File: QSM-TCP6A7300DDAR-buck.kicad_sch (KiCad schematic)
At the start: 20 parts, among them U1 TCP6A7300DDAR

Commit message: docs: identificar trazos críticos en el esquemático para ruteo
Se agregaron colores y leyendas para diferenciar las pistas de alta corriente (rojo), señales sensibles de retroalimentación (amarillo) y nodos ruidosos con alto dv/dt. Sirve como guía visual obligatoria para el diseño del PCB.
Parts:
- removed U1: TCP6A7300DDAR, Package_SO_ARR:SOIC-8-1EP_3.9x4.9mm_P1.27mm_EP2.29x3mm_ThermalVias, symbol Power_IC_SMD_ARR:TCP6A7300DDAR
- added U1: TCP6A7300DDAR, Package_SO_ARR:SOIC-8-1EP_3.9x4.9mm_P1.27mm_EP2.29x3mm_ThermalVias, symbol SMPS_SMD_ARR:TCP6A7300DDAR
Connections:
- net GND: now also U1.7 (GND), U1.9 (GND)
- net at C5.2, L1.1: now also U1.8 (SW)
- net at C1.1, C2.1, C7.1: now also U1.2 (VIN), U1.3 (EN)
- net at C5.1: now also U1.1 (BOOT)
- net at C6.2, R1.2, R2.1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: now also U1.5 (FB)
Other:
- note added: "HIGH CURRENT TRACES"
- note added: "MOST NOISE SENSITIVE, SMALL SIGNAL TRACES"
- note added: "NOISY, HIGH dv/dt NODES/TRACES"

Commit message: docs: agregar lista de materiales (BOM) y límites de hardware
Se integró la tabla de componentes críticos con enlaces a proveedores locales para ensamble rápido. También se documentaron las consideraciones de derating físico: límite de corriente de 1.4A por saturación del inductor y pérdida de capacitancia por DC bias en los cerámicos 0805.
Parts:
- L1: footprint (none) -> IND_SMD_ARR:IND_SWPA6020S_SNL
- R1: Supplier 1 (none) -> https://uelectronics.com/producto/resistor-56k-ohm-1-8w-smd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
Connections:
- net at C3.1, C4.1, C6.1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: now also R4.1
- no-connect marks 2 -> 1
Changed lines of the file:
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@@
 	)
 	(junction
-		(at 110.49 86.36)
-		(diameter 0)
-		(color 108 0 2 1)
-	)
-	(junction
 		(at 111.76 73.66)
 		(diameter 0)
@@
 	)
 	(junction
+		(at 162.56 81.28)
+		(diameter 0)
+		(color 0 0 0 0)
+	)
+	(junction
 		(at 208.28 76.2)
 		(diameter 0)
@@
 	)
 	(junction
+		(at 162.56 76.2)
+		(diameter 0)
+		(color 108 0 2 1)
+	)
+	(junction
 		(at 162.56 96.52)
 		(diameter 0)
@@
 	)
 	(junction
+		(at 110.49 86.36)
+		(diameter 0)
+		(color 108 0 2 1)
+	)
+	(junction
 		(at 76.2 73.66)
 		(diameter 0)
@@
 	)
 	(junction
-		(at 157.48 76.2)
-		(diameter 0)
-		(color 108 0 2 1)
-	)
-	(junction
 		(at 101.6 73.66)
 		(diameter 0)
@@
 	)
 	(no_connect
-		(at 162.56 81.28)
-	)
-	(no_connect
 		(at 132.08 83.82)
 	)
 	(wire
 		(pts
+			(xy 157.48 81.28) (xy 162.56 81.28)
+		)
+		(stroke
+			(width 0)
+			(type default)
+		)
+	)
+	(wire
+		(pts
 			(xy 132.08 73.66) (xy 133.35 73.66)
 		)
@@
 	(wire
 		(pts
-			(xy 154.94 76.2) (xy 157.48 76.2)
+			(xy 154.94 76.2) (xy 162.56 76.2)
 		)
 		(stroke
@@
 	(wire
 		(pts
-			(xy 110.49 86.36) (xy 110.49 91.44)
+			(xy 110.49 86.36) (xy 110.49 87.63)
 		)
 		(stroke
@@
 	(wire
 		(pts
-			(xy 170.18 96.52) (xy 177.8 96.52)
+			(xy 143.51 71.12) (xy 143.51 76.2)
 		)
 		(stroke
 			(width 0.381)
 			(type default)
-			(color 255 244 0 1)
+			(color 108 0 2 1)
 		)
 	)
 	(wire
 		(pts
-			(xy 143.51 71.12) (xy 143.51 76.2)
+			(xy 208.28 86.36) (xy 208.28 90.17)
 		)
 		(stroke
@@
 	(wire
 		(pts
-			(xy 208.28 86.36) (xy 208.28 90.17)
+			(xy 140.97 71.12) (xy 143.51 71.12)
 		)
 		(stroke
@@
 	(wire
 		(pts
-			(xy 140.97 71.12) (xy 143.51 71.12)
+			(xy 170.18 93.98) (xy 170.18 96.52)
 		)
 		(stroke
 			(width 0.381)
 			(type default)
-			(color 108 0 2 1)
+			(color 255 244 0 1)
 		)
 	)
 	(wire
 		(pts
-			(xy 170.18 93.98) (xy 170.18 96.52)
+			(xy 110.49 83.82) (xy 110.49 86.36)
 		)
 		(stroke
 			(width 0.381)
 			(type default)
-			(color 255 244 0 1)
+			(color 108 0 2 1)
 		)
 	)
 	(wire
 		(pts
-			(xy 110.49 83.82) (xy 110.49 86.36)
+			(xy 162.56 76.2) (xy 170.18 76.2)
 		)
 		(stroke
@@
 	(wire
 		(pts
+			(xy 157.48 87.63) (xy 157.48 81.28)
+		)
+		(stroke
+			(width 0)
+			(type default)
+		)
+	)
+	(wire
+		(pts
 			(xy 220.98 76.2) (xy 208.28 76.2)
 		)
@@
 		)
 	)
-	(wire
+	(polyline
 		(pts
-			(xy 157.48 76.2) (xy 170.18 76.2)
+			(xy 29.21 142.24) (xy 30.48 140.97)
 		)
 		(stroke
-			(width 0.381)
-			(type default)
-			(color 108 0 2 1)
+			(width 0.254)
+			(type solid)
 		)
 	)
 	(wire
 		(pts
-			(xy 157.48 76.2) (xy 157.48 87.63)
+			(xy 170.18 96.52) (xy 177.8 96.52)
 		)
 		(stroke
-			(width 0)
+			(width 0.381)
 			(type default)
-		)
-	)
-	(polyline
-		(pts
-			(xy 29.21 142.24) (xy 30.48 140.97)
-		)
-		(stroke
-			(width 0.254)
-			(type solid)
+			(color 255 244 0 1)
 		)
 	)
@@
 		)
 	)
+	(wire
+		(pts
+			(xy 162.56 76.2) (xy 162.56 81.28)
+		)
+		(stroke
+			(width 0)
+			(type default)
+		)
+	)
 	(symbol
 		(lib_id "Power_sym_ARR:GND")
@@
 			)
 		)
-		(property "Footprint" ""
+		(property "Footprint" "IND_SMD_ARR:IND_SWPA6020S_SNL"
 			(at 146.05 76.2 0)
 			(hide yes)
@@
 			)
 		)
+		(property "Supplier 1" "https://uelectronics.com/producto/resistor-56k-ohm-1-8w-smd-0805-rs-05k6802ft/"
+			(at 170.18 90.17 0)
+			(hide yes)
+			(show_name no)
+			(do_not_autoplace no)
+			(effects
+				(font
+					(size 1.27 1.27)
+				)
+			)
+		)
 		(pin "1"
 		)
@@
 	(symbol
 		(lib_id "Power_sym_ARR:GND")
-		(at 110.49 93.98 0)
+		(at 110.49 90.17 0)
 		(unit 1)
 		(body_style 1)
@@
 		(fields_autoplaced yes)
 		(property "Reference" "#PWR01"
-			(at 110.49 90.17 0)
+			(at 110.49 86.36 0)
 			(hide yes)
 			(show_name no)
@@
 		)
 		(property "Value" "GND"
-			(at 110.49 99.06 0)
+			(at 110.49 95.25 0)
 			(hide yes)
 			(show_name no)
@@
 		)
 		(property "Footprint" ""
-			(at 110.49 93.98 0)
+			(at 110.49 90.17 0)
 			(hide yes)
 			(show_name no)
@@
 		)
 		(property "Datasheet" ""
-			(at 110.49 93.98 0)
+			(at 110.49 90.17 0)
 			(hide yes)
 			(show_name no)
@@
 		)
 		(property "Description" ""
-			(at 110.49 93.98 0)
+			(at 110.49 90.17 0)
 			(hide yes)
 			(show_name no)

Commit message: feat: agregar test points en nodos críticos y referencias de filtros EMI
Se colocaron Test Points estratégicos en el esquemático (ej. VIN, VOUT, SW y el lazo de Feedback) para facilitar las mediciones con osciloscopio y la inyección de señal. Además, se actualizó el README.md con la bibliografía de Texas Instruments sobre el Criterio de Middlebrook y el amortiguamiento de filtros LC de segunda etapa.
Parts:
- added C10, C11, C9: 0.1uF, Capacitor_SMD_ARR:C_0805_2012Metric, symbol Passive_ARR:C_Generic
- added FB1, FB2: (no value), Resistor_SMD_ARR:R_0805_2012Metric, symbol Passive_ARR:FB_Generic
- added J1, J2: 691322310002, 691322310002:691322310002, symbol Connector_THT_ARR:691322310002
- added TP1, TP2, TP3, TP4, TP5, TP6: TestPoint, symbol Passive_ARR:TestPoint
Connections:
- net GND: now also C10.2, C11.2, C9.2, J1.1, J2.2, TP6.1
- net at C5.2, L1.1, U1.8 (SW): now also TP3.1
- net at C3.1, C4.1, C6.1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: now also FB2.1, TP4.1
- net at C1.1, C2.1, C7.1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: now also C10.1, FB1.2, TP2.1
- net at C6.2, R1.2, R2.1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: now also TP5.1
- new net: C11.1, FB2.2, J2.1
- new net: C9.1, FB1.1, J1.2, TP1.1
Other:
- moved on the sheet: C1, C2, C3, C4, C5, C6, C7, C8, L1, R1, R2, R3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

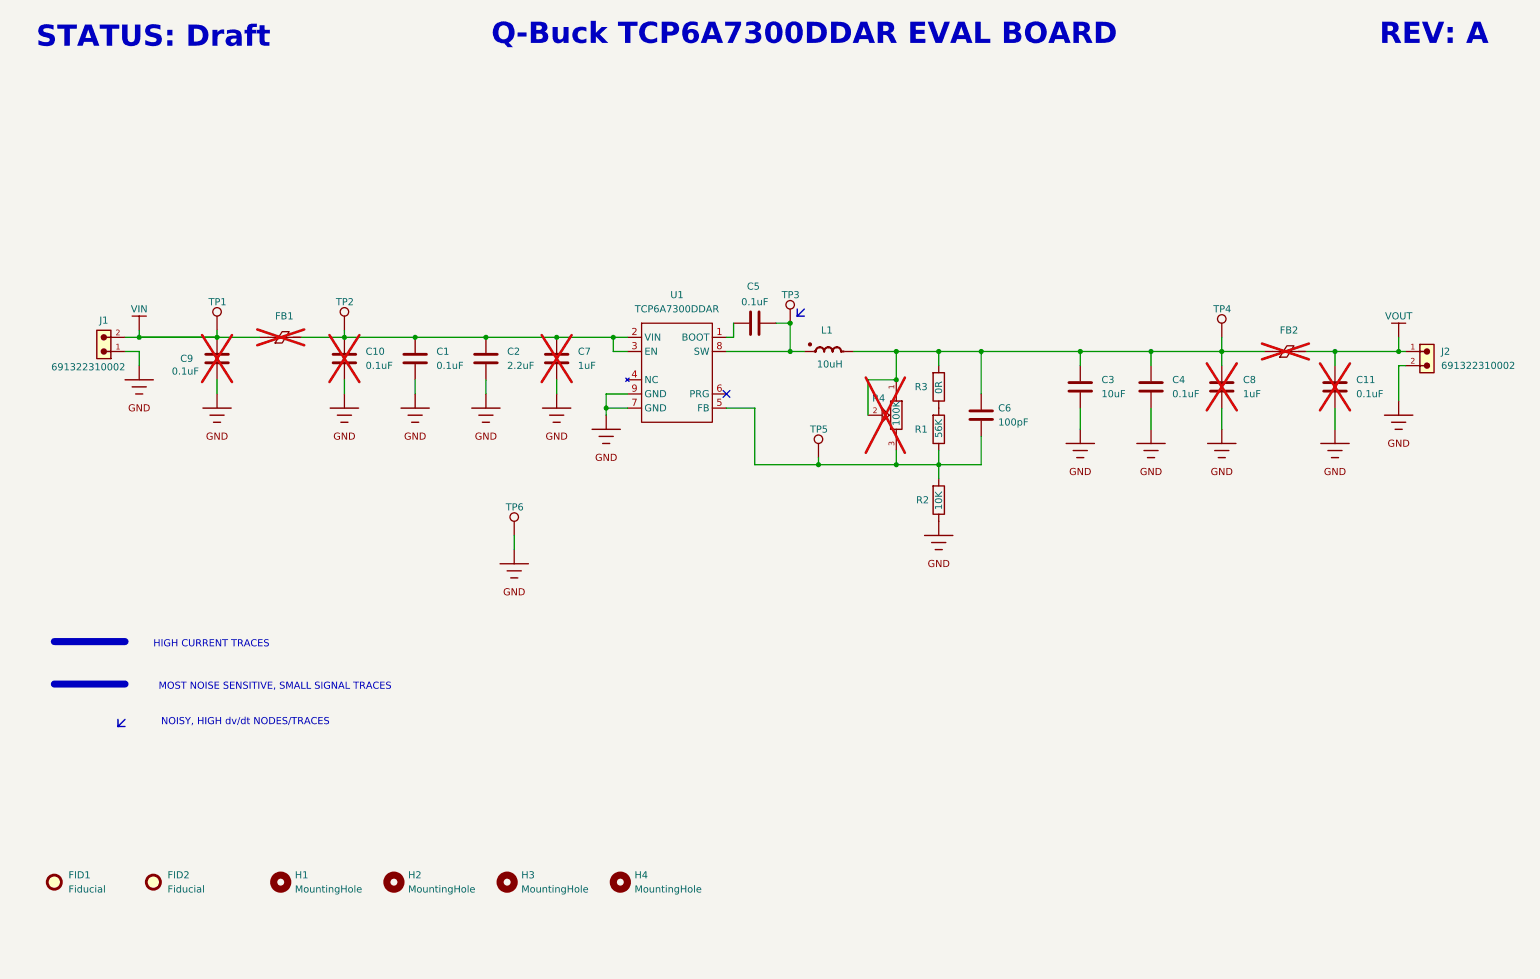
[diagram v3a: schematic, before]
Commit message: feat(layout): [WIP] ruteo inicial de polígonos de potencia en 4 capas
Se definió el stackup simétrico de 4 capas (SIG-GND-GND-SIG) y se realizó el floorplanning. Se trazaron los polígonos preliminares de alta corriente (VIN, SW, VOUT) en la capa Top. El ruteo de la señal de Feedback y los planos de tierra internos siguen en progreso.
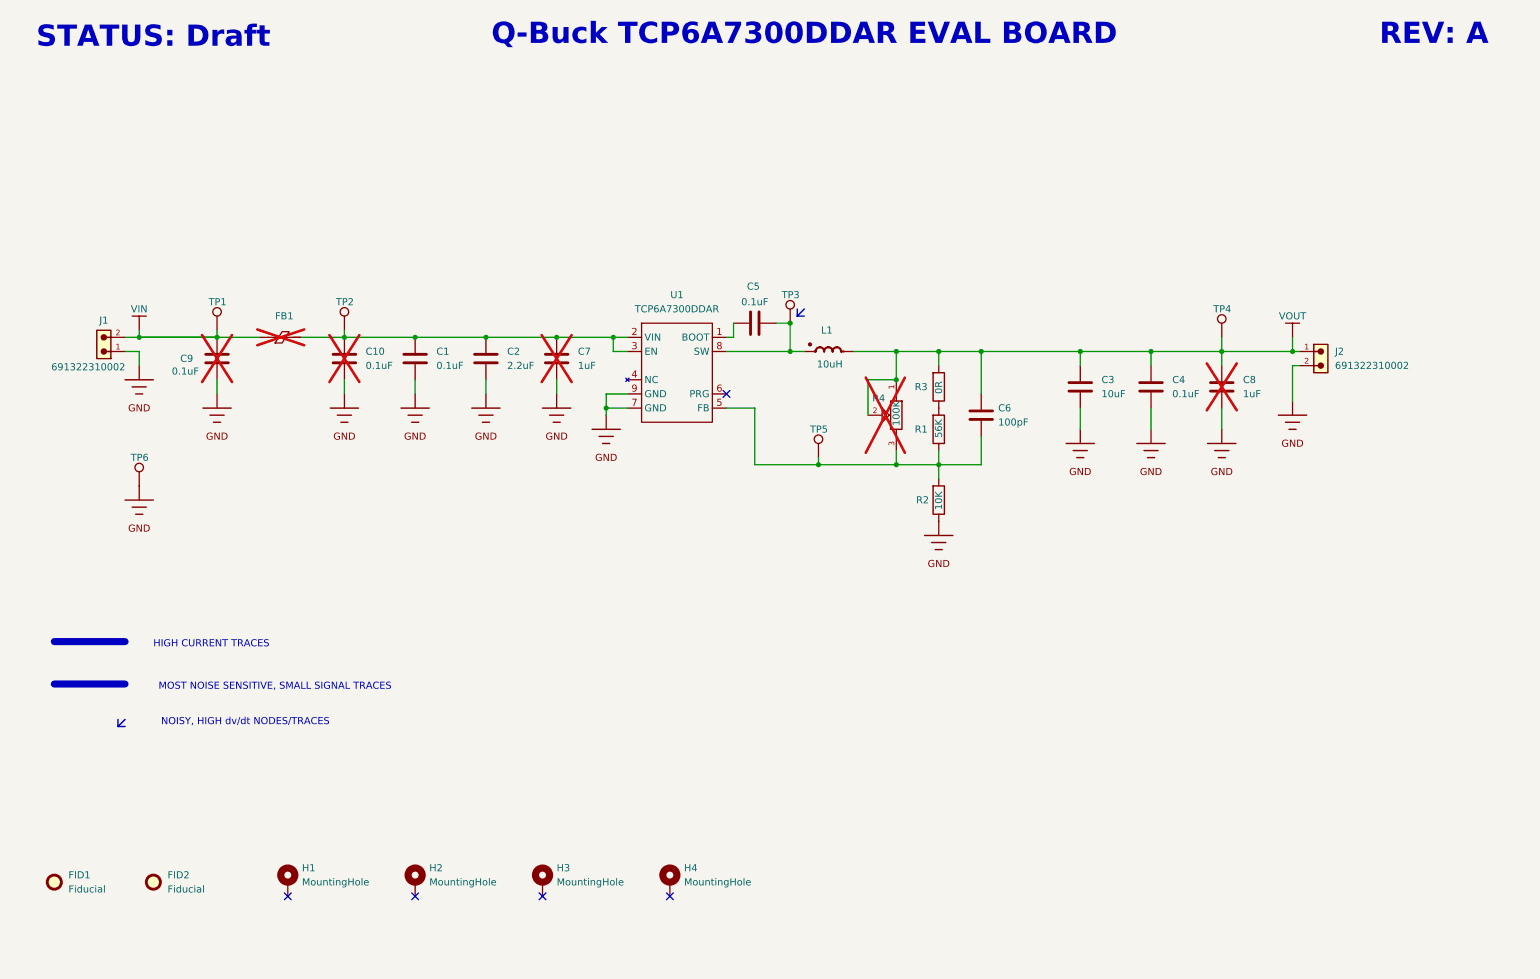
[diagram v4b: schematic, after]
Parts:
- removed C11: 0.1uF, Capacitor_SMD_ARR:C_0805_2012Metric, symbol Passive_ARR:C_Generic
- removed FB2: (no value), Resistor_SMD_ARR:R_0805_2012Metric, symbol Passive_ARR:FB_Generic
- removed H1, H2, H3, H4: MountingHole, symbol Mechanical_ARR:MountingHole
- added H1, H2, H3, H4: MountingHole, Mounting_Hole_ARR:MountingHole_3.2mm_M3_Pad_Via, symbol Mechanical_ARR:MountingHole_conn
- FID1, FID2: footprint Fiducial_ARR:Fiducial_0.75mm_Mask2.25mm -> Fiducial_ARR:Fiducial_0.5mm_Mask1.5mm
- J1, J2: footprint 691322310002:691322310002 -> Connector_THT_ARR:691322310002
- R4: footprint Resistor_THT_ARR:TRIM_3362P-1-503LF -> Resistor_THT_ARR:POT_TC33_3X3P8_BRN; Part number 3362P -> TC33X-2-103E; Supplier 1 https://uelectronics.com/producto/potenciometro-de-precisio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 -> https://uelectronics.com/producto/trimpot-smd-10k-ohm-3x3-8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
- TP1, TP2, TP3, TP4, TP5, TP6: footprint (none) -> Test_Point_ARR:TestPoint_Pad_D1.0mm
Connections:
- net at J2.1: now also C3.1, C4.1, C6.1, C8.1, L1.2, R3.1, R4.1, R4.2, TP4.1
- no-connect marks 1 -> 5
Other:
- moved on the sheet: J2, TP6

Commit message: feat(hardware): optimización de hot-loops, conector de inyección de señal y actualización de docs
Esquemático y PCB:
- Reubicación jerárquica de capacitores de entrada y salida para minimizar el área del Hot Loop y reducir el ESL, alineado a notas de aplicación de PI.
- Adición de conector SMD JST SH (BM02B-SRSS-TB) en paralelo a la resistencia de inyección para facilitar la medición del lazo de control (Bode Plot).

Documentación (README):
- Integración de 'badges' de estado y especificaciones técnicas.
- Redacción de la justificación técnica del layout (Control EMI y Hot Loops) referenciando bibliografía de TI.
- Adición de render 3D de la placa y diagrama esquemático de la aplicación típica.
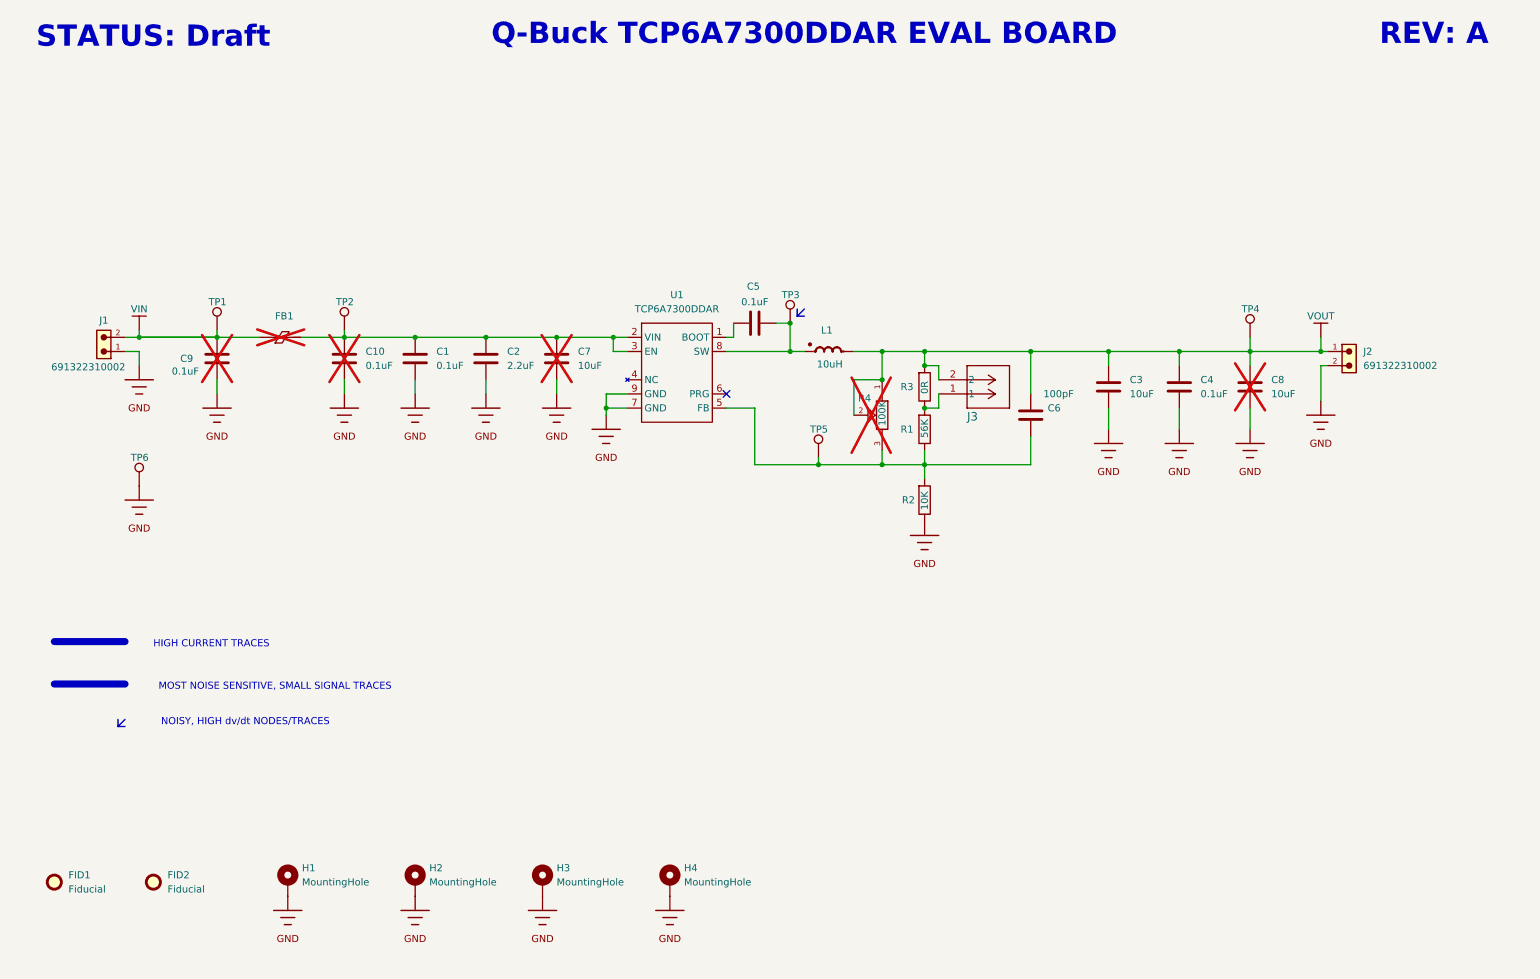
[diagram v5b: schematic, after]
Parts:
- added J3: BM02B-SRSS-TB LFSN, Connector_SMD_ARR:BM02B-SRSS-TB_JST, symbol Connector_SMD_ARR:BM02B-SRSS-TB_LFSN
- C7, C8: value 1uF -> 10uF; footprint Capacitor_SMD_ARR:C_0805_2012Metric -> Capacitor_SMD_ARR:C_1206_3216Metric; Manufacturer CCTC -> Samsung; Package 0805 -> 1206; Part number TCC0805X7R105K500DTS -> CL31B106KBHNNNE; Supplier 1 https://uelectronics.com/producto/capacitor-ceramico-0805-1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 -> https://uelectronics.com/producto/cl31b106kbhnnne-capacitor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
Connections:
- net GND: now also H1.1, H2.1, H3.1, H4.1
- net at C3.1, C4.1, C6.1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: now also J3.2
- net at R1.1, R3.2: now also J3.1
- no-connect marks 5 -> 1
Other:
- moved on the sheet: C3, C4, C6, J2, R1, R2, R3, R4, TP4
